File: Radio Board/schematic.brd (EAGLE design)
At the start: 55 x 72.5 mm, 13 parts, among them J1 132134RP

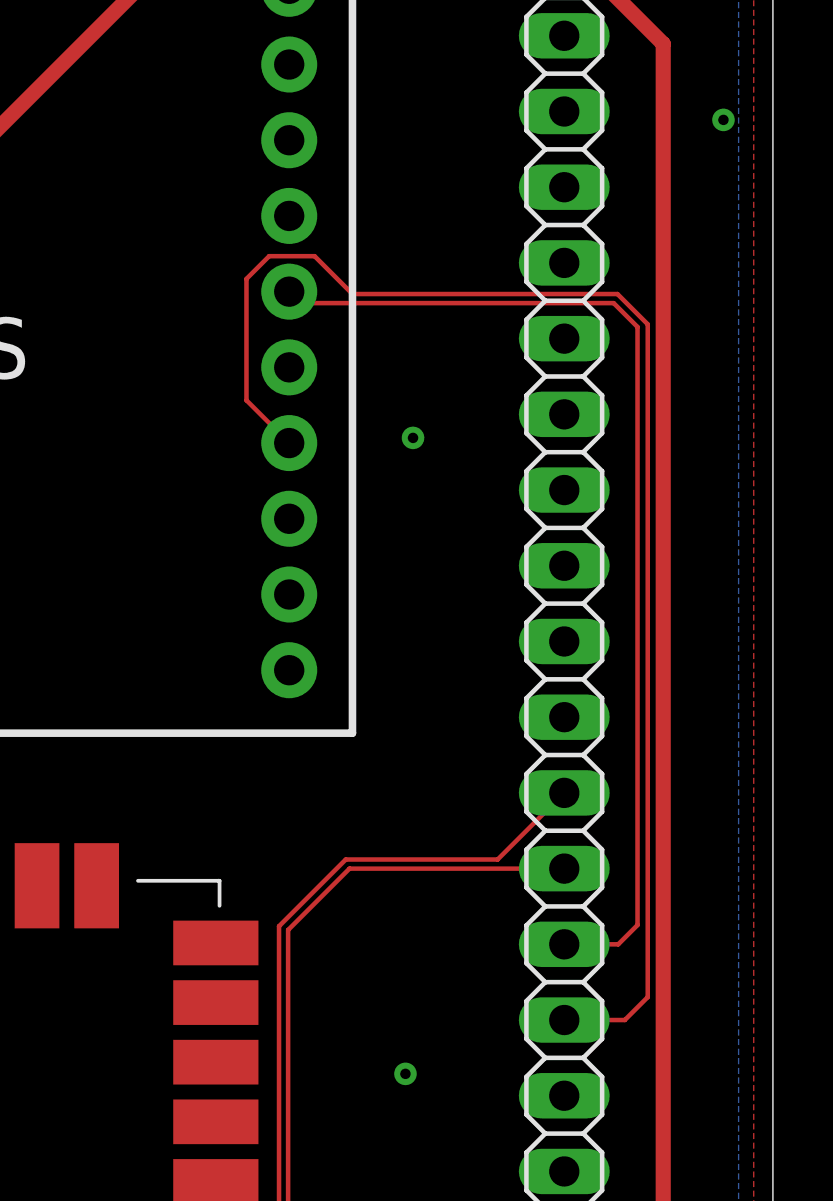
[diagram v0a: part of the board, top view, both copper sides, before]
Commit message: switched from using rxa to rxb
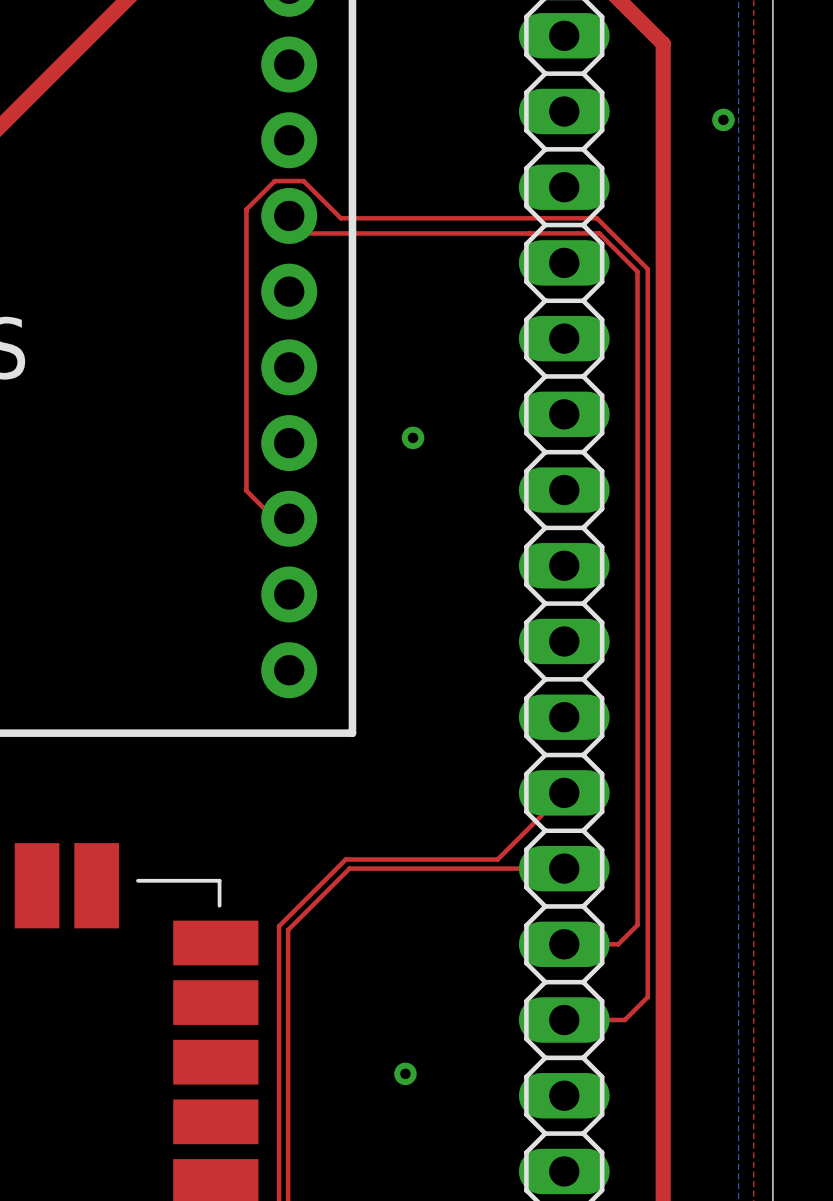
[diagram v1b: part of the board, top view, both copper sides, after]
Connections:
- net RX1: now also GPS.8; no longer GPS.7
- net TX1: now also GPS.4; no longer GPS.5
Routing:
- net RX1: track 46.5 -> 53.9 mm
- net TX1: track 35.0 -> 37.1 mm
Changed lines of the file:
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@@
 <drawing>
 <settings>
-<setting alwaysvectorfont="yes"/>
+<setting alwaysvectorfont="no"/>
 <setting verticaltext="up"/>
 </settings>
@@
 <signal name="RX1">
 <contactref element="JP1" pad="7"/>
-<contactref element="GPS" pad="7"/>
-<wire x1="50.8" y1="34.578" x2="50.032" y2="33.81" width="0.1524" layer="1"/>
+<wire x1="50.032" y1="33.81" x2="50.8" y2="34.578" width="0.1524" layer="1"/>
 <wire x1="50.032" y1="33.81" x2="48" y2="33.81" width="0.1524" layer="1"/>
-<wire x1="50.8" y1="34.578" x2="50.8" y2="57.15" width="0.1524" layer="1"/>
-<wire x1="40.894" y1="58.166" x2="39.624" y2="59.436" width="0.1524" layer="1"/>
-<wire x1="39.624" y1="59.436" x2="38.1" y2="59.436" width="0.1524" layer="1"/>
-<wire x1="38.1" y1="59.436" x2="37.338" y2="58.674" width="0.1524" layer="1"/>
-<wire x1="37.338" y1="58.674" x2="37.338" y2="54.6" width="0.1524" layer="1"/>
-<wire x1="37.338" y1="54.6" x2="38.772" y2="53.166" width="0.1524" layer="1"/>
-<wire x1="50.8" y1="57.15" x2="49.784" y2="58.166" width="0.1524" layer="1"/>
-<wire x1="49.784" y1="58.166" x2="40.894" y2="58.166" width="0.1524" layer="1"/>
+<contactref element="GPS" pad="8"/>
+<wire x1="39.25596875" y1="61.9544" x2="38.28803125" y2="61.9544" width="0.1524" layer="1"/>
+<wire x1="40.50436875" y1="60.706" x2="39.25596875" y2="61.9544" width="0.1524" layer="1"/>
+<wire x1="50.8" y1="59.00398125" x2="49.09798125" y2="60.706" width="0.1524" layer="1"/>
+<wire x1="49.09798125" y1="60.706" x2="40.50436875" y2="60.706" width="0.1524" layer="1"/>
+<wire x1="50.8" y1="34.578" x2="50.8" y2="59.00398125" width="0.1524" layer="1"/>
+<wire x1="37.338" y1="60.96" x2="37.338" y2="51.562" width="0.1524" layer="1"/>
+<wire x1="37.338" y1="51.562" x2="38.274" y2="50.626" width="0.1524" layer="1"/>
+<wire x1="38.274" y1="50.626" x2="38.772" y2="50.626" width="0.1524" layer="1"/>
+<wire x1="38.28803125" y1="61.9544" x2="37.338" y2="61.00436875" width="0.1524" layer="1"/>
+<wire x1="37.338" y1="61.00436875" x2="37.338" y2="60.96" width="0.1524" layer="1"/>
 </signal>
 <signal name="TX1">
 <contactref element="JP1" pad="8"/>
-<contactref element="GPS" pad="5"/>
 <wire x1="49.812" y1="36.35" x2="48" y2="36.35" width="0.1524" layer="1"/>
 <wire x1="49.812" y1="36.35" x2="50.457471875" y2="36.995471875" width="0.1524" layer="1"/>
-<wire x1="50.457471875" y1="36.995471875" x2="50.457471875" y2="57.061471875" width="0.1524" layer="1"/>
-<wire x1="50.457471875" y1="57.061471875" x2="49.65774375" y2="57.8612" width="0.1524" layer="1"/>
-<wire x1="39.1568" y1="57.8612" x2="38.772" y2="58.246" width="0.1524" layer="1"/>
-<wire x1="49.65774375" y1="57.8612" x2="39.1568" y2="57.8612" width="0.1524" layer="1"/>
+<contactref element="GPS" pad="4"/>
+<wire x1="49.172325" y1="60.2006" x2="46.827675" y2="60.2006" width="0.1524" layer="1"/>
+<wire x1="46.827675" y1="60.2006" x2="46.825075" y2="60.198" width="0.1524" layer="1"/>
+<wire x1="50.457471875" y1="58.915453125" x2="49.172325" y2="60.2006" width="0.1524" layer="1"/>
+<wire x1="39.36" y1="60.198" x2="38.772" y2="60.786" width="0.1524" layer="1"/>
+<wire x1="50.457471875" y1="36.995471875" x2="50.457471875" y2="58.915453125" width="0.1524" layer="1"/>
+<wire x1="46.825075" y1="60.198" x2="39.36" y2="60.198" width="0.1524" layer="1"/>
 </signal>
 <signal name="RX2">

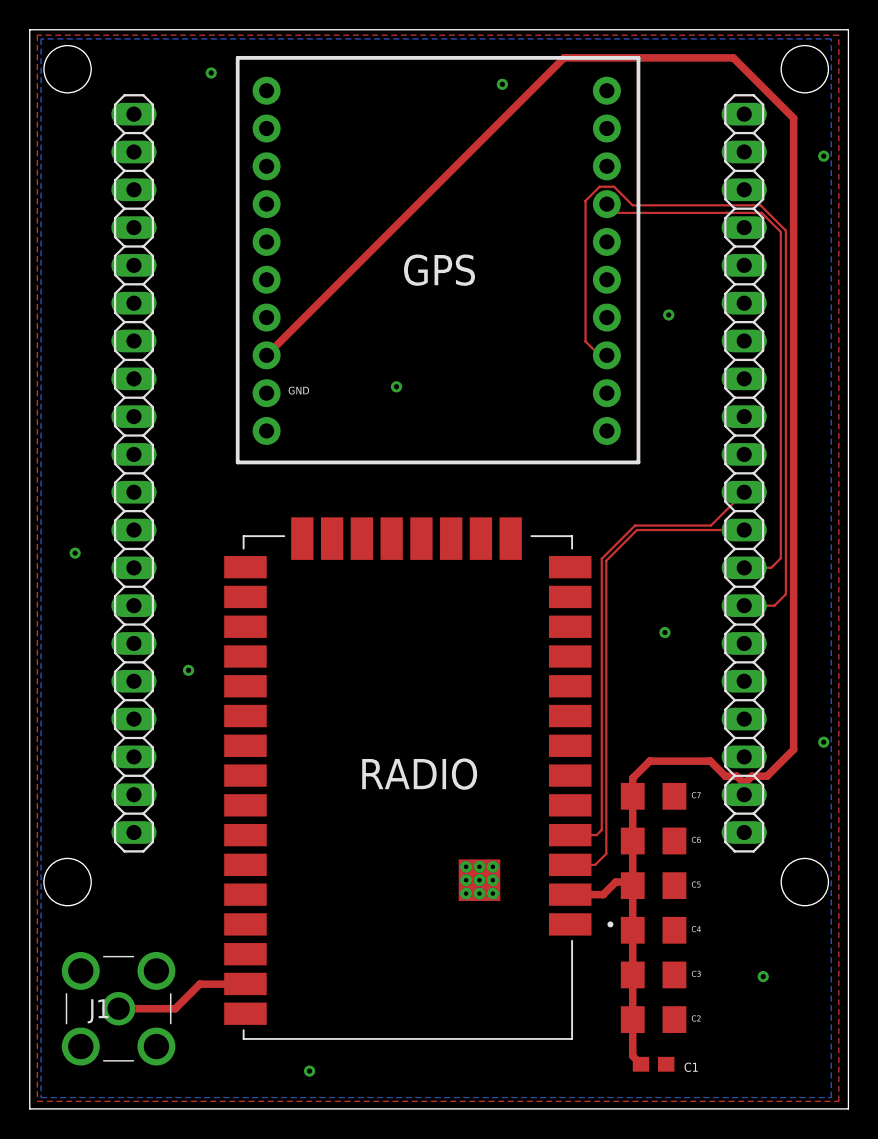
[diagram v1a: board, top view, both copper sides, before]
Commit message: fixed wiring on radio board
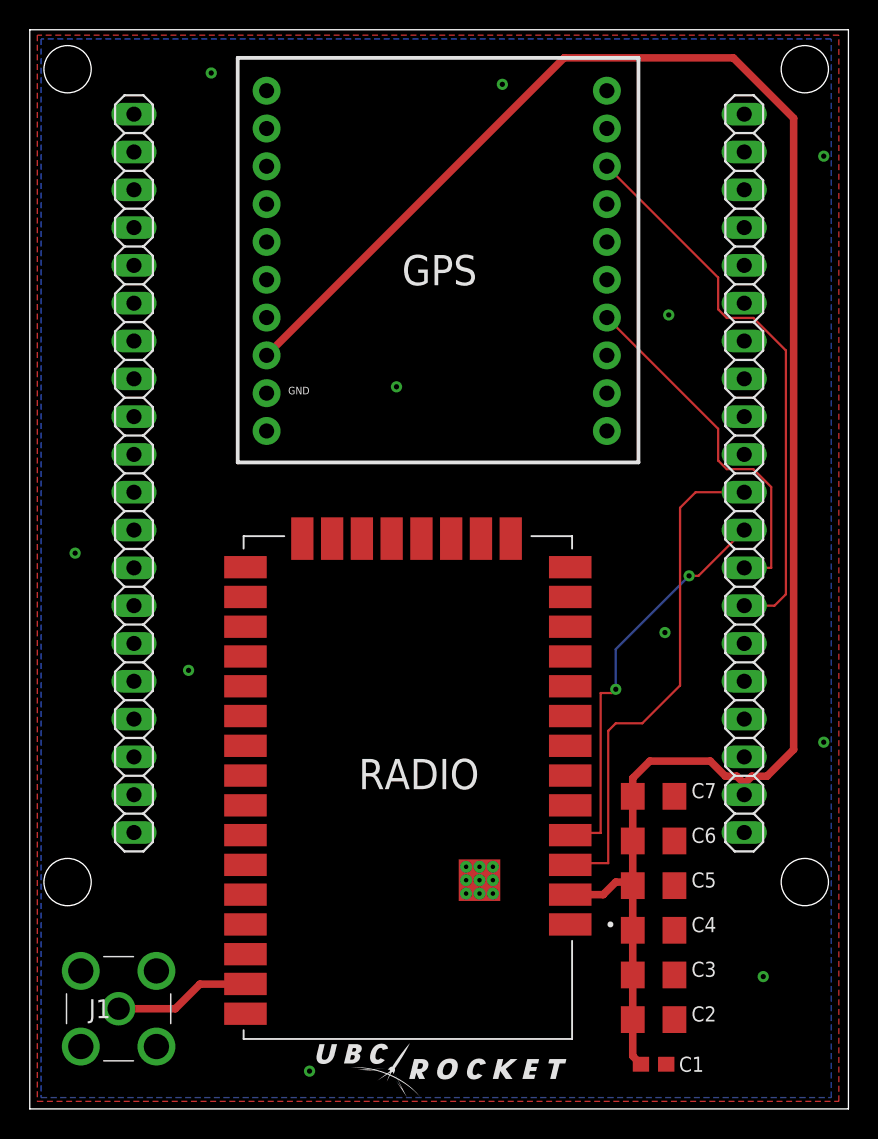
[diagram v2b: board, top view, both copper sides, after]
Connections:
- net RX1: now also GPS.3; no longer GPS.8
- net RX2: now also RADIO.4; no longer RADIO.3
- net TX1: now also GPS.7; no longer GPS.4
- net TX2: now also RADIO.3; no longer RADIO.4
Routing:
- net RX1: track 53.9 -> 37.9 mm
- net TX1: track 37.1 -> 24.2 mm
- net RX2: track 32.5 -> 26.2 mm, vias 0 -> 2
- net TX2: track 31.9 -> 33.2 mm
